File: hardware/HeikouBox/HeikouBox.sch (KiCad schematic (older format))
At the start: 93 parts, among them J1 USB_B_Micro, J103 JTAG, J2 Micro_SD_Card_Det, Q1 AO3400, Q2 AO3400, Q3 AO3400, SW1 RESET, U1 HeikouBox-Core, U2 K4S281632-UC60, U3 LD1117(1.2V), U4 LD1117(3.3V), U5 74HC04D, U6 LD1117(2.5V), U7 ATmega32U4-AU, Y1 14.31818MHz, Y2 28.37516MHz, Y3 8M

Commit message: Update to local libraries, minor work
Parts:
- U1: symbol KasaneK-Custom-Parts:HeikouBox-Core -> ksk-heikoubox:HeikouBox-Core
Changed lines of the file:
@@
 EESchema Schematic File Version 4
-LIBS:HeikouBox-cache
-EELAYER 26 0
+EELAYER 30 0
 EELAYER END
 $Descr A3 16535 11693
@@
 	6700 4300 6900 4300
 $Comp
-L KasaneK-Custom-Parts:HeikouBox-Core U1
+L ksk-heikoubox:HeikouBox-Core U1
 U 1 1 5F328BCC
 P 14200 3300
@@
 $EndComp
 $Comp
-L KasaneK-Custom-Parts:HeikouBox-Core U1
-U 2 1 5F328D2B
+L ksk-heikoubox:HeikouBox-Core U1
+U 1 1 5F328D2B
 P 14200 4900
 F 0 "U1" H 14600 5065 50  0000 C CNN
@@
 F 2 "" H 14500 4900 50  0001 C CNN
 F 3 "" H 14500 4900 50  0001 C CNN
-	2    14200 4900
-	1    0    0    -1
-$EndComp
-$Comp
-L KasaneK-Custom-Parts:HeikouBox-Core U1
-U 3 1 5F328EEB
+	1    14200 4900
+	1    0    0    -1
+$EndComp
+$Comp
+L ksk-heikoubox:HeikouBox-Core U1
+U 1 1 5F328EEB
 P 14200 6500
 F 0 "U1" H 14600 6665 50  0000 C CNN
@@
 F 2 "" H 14500 6500 50  0001 C CNN
 F 3 "" H 14500 6500 50  0001 C CNN
-	3    14200 6500
-	1    0    0    -1
-$EndComp
-$Comp
-L KasaneK-Custom-Parts:HeikouBox-Core U1
-U 4 1 5F329004
+	1    14200 6500
+	1    0    0    -1
+$EndComp
+$Comp
+L ksk-heikoubox:HeikouBox-Core U1
+U 1 1 5F329004
 P 14200 8100
 F 0 "U1" H 14600 8265 50  0000 C CNN
@@
 F 2 "" H 14500 8100 50  0001 C CNN
 F 3 "" H 14500 8100 50  0001 C CNN
-	4    14200 8100
-	1    0    0    -1
-$EndComp
+	1    14200 8100
+	1    0    0    -1
+$EndComp

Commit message: Core: Create/use overall footprint again
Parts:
- U1: symbol ksk-heikoubox:HeikouBox-Core -> KSK_HeikouBox:HeikouBox_Core
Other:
- moved on the sheet: C10, C11, C8, C9, J103, R10, R11, R12, R13, R14, R15, R16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

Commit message: Initial mainboard v1.0 schematic finished
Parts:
- removed C11: 105, symbol Device:C
- removed D3: BAT54S, Package_TO_SOT_SMD:SOT-23, symbol Diode:BAT54S
- removed JP1: 1, symbol Jumper:SolderJumper_2_Bridged
- removed JP2: 2, symbol Jumper:SolderJumper_2_Bridged
- removed JP3: 3, symbol Jumper:SolderJumper_2_Bridged
- removed JP4: 6, symbol Jumper:SolderJumper_2_Bridged
- removed JP5: 7, symbol Jumper:SolderJumper_2_Bridged
- removed Q1, Q2, Q3: AO3400, symbol Device:Q_NMOS_GSD
- removed R1: 100, symbol Device:R
- removed R3: 10K, symbol Device:R
- removed U2: K4S281632-UC60, TSOPII-54, symbol Memory_RAM:AS4C4M16SA
- removed U7: ATmega32U4-AU, Package_QFP:TQFP-44_10x10mm_P0.8mm, symbol MCU_Microchip_ATmega:ATmega32U4-AU
- added C1, C24, C25, C26, C27, C3, C31, C32, C33, C34, C35, C6, C8: 100n, symbol Device:C
- added C10, C16, C17: 10u, symbol Device:C
- added C14: 22p, symbol Device:C
- added C19: 10n, symbol Device:C
- added C21, C22, C23: 1u, symbol Device:C
- added D1: DEBUG, symbol Device:LED
- added DS1: OLED-4P-I2C, symbol KSK_HeikouBox:OLED-4P-I2C
- added F1: Poly 0.5A, symbol Device:Polyfuse_Small
- added J1: VGA, symbol Connector:DB15_Female_HighDensity_MountingHoles
- added J10: XBUS, symbol Connector_Generic:Conn_01x16
- added J2: PJ307, symbol Connector:AudioJack3_SwitchTR
- added J6: 5VDC, symbol Connector:Barrel_Jack_Switch
- added J7: Gamepad 1, symbol Connector_Generic:Conn_01x07
- added J8: Gamepad 2, symbol Connector_Generic:Conn_01x07
- added J9: Keyboard, symbol Connector:Mini-DIN-6
- added JP1: JACK - USB, symbol Jumper:SolderJumper_3_Bridged12
- added Q1, Q2, Q3, Q4, Q5, Q6, Q7: MMBT3904, Package_TO_SOT_SMD:SOT-23, symbol Transistor_BJT:MMBT3904
- added Q10, Q11, Q12, Q13, Q14, Q9: BSS138, Package_TO_SOT_SMD:SOT-23, symbol Transistor_FET:BSS138
- added Q8: MMBT3906, Package_TO_SOT_SMD:SOT-23, symbol Transistor_BJT:MMBT3906
- added R10, R105, R115, R117, R119, R121, R123, R125, R14, R15, R16, R17, R18, R19, R20, R24, R5, R52, R53, R54, R55, R56, R57, R58, R59, R6, R60, R61, R62, R7, R70, R8: 2K2, symbol Device:R
- added R100, R107, R109, R111, R113, R114, R116, R118, R120, R122, R124, R73, R74, R75, R76, R77, R78: 10K, symbol Device:R
- added R101, R102, R103, R104, R106, R108, R110, R112, R22, R4, R63, R66, R68, R72, R79, R80, R91, R92, R93, R94, R95, R96, R97, R99: 1K, symbol Device:R
- added R64: 75R, symbol Device:R
- added RV1, RV2, RV3: 1K, symbol Device:R_POT_TRIM
- added SW2: Up, symbol Switch:SW_Push
- added SW3: Select, symbol Switch:SW_Push
- added SW4: Down, symbol Switch:SW_Push
- added U2: SDRAM 128Mbit, Package_SO:TSOP-II-54_22.2x10.16mm_P0.8mm, symbol Memory_RAM:W9812G6KH-6
- added U7: ATmega644PA-AU, Package_QFP:TQFP-44_10x10mm_P0.8mm, symbol MCU_Microchip_ATmega:ATmega644PA-AU
- added U8: MCP2221AxSL, Package_SO:SOIC-14_3.9x8.7mm_P1.27mm, symbol Interface_USB:MCP2221AxSL
- C11: renamed from C12; value 220 -> 22p
- C12: renamed from C14; value 220 -> 22p
- C13: value 220 -> 22p
- C15: value 220 -> 100n
- C18: renamed from C8; value 472 -> 10n
- C2: value 106 -> 100n
- C20: renamed from C10; value 105 -> 1u
- C28: renamed from C5; value 104 -> 100n
- C29: renamed from C6; value 220 -> 22p
- C30: renamed from C7; value 220 -> 22p
- C4: value 105 -> 100n
- C5: renamed from C1; value 106 -> 10u
- C7: renamed from C3; value 106 -> 10u
- C9: value 472 -> 10u
- R1: renamed from R20; value 330K -> 1M
- R12, R13, R25: value 10K -> 2K2
- R2: value 10K -> 1K
- R21: value 100 -> 2K2
- R23: value 1K -> 75R
- R3: renamed from R21; value 330K -> 1M
- R44: value 2K2 -> 1K
- R45: value 2K2 -> 75R
- R50, R51: value 22 -> 2K2
- R65: renamed from R20; value 100 -> 1K
- R67: renamed from R24; value 10K -> 1K
- R69: renamed from R22; value 1K -> 2K2
- R71: renamed from R10; value 2K2 -> 1K
- R81: renamed from R14; value 2K2 -> 10K
- R82: renamed from R15; value 2K2 -> 10K
- R83: renamed from R16; value 2K2 -> 10K
- R84: renamed from R17; value 2K2 -> 10K
- R85: renamed from R18; value 2K2 -> 10K
- R86: renamed from R19; value 2K2 -> 10K
- R87: renamed from R4; value 2K2 -> 1K
- R88: renamed from R5; value 2K2 -> 1K
- R89: renamed from R6; value 2K2 -> 1K
- R9: value 1K -> 2K2
- R90: renamed from R7; value 2K2 -> 1K
- SW1: value RESET -> Reset; footprint Connector_PinHeader_2.54mm:PinHeader_1x02_P2.54mm_Vertical -> (none)
- U1: symbol KSK_HeikouBox:HeikouBox_Core -> KSK_HeikouBox:HeikouBox-Core
- U3: renamed from U4; value LD1117(3.3V) -> LD1117S33TR
- U4: renamed from U3; value LD1117(1.2V) -> LD1117S12TR
- U5: renamed from U6; value LD1117(2.5V) -> LD1117S25TR; symbol Regulator_Linear:LD1117S33TR_SOT223 -> Regulator_Linear:LD1117S25TR_SOT223
- U6: renamed from U5; value 74HC04D -> 74HCU04
- U6: renamed from U5; value MC74HCU04AD -> 74HCU04
- Y1: value 14.31818MHz -> 14.31818M
- Y2: value 28.37516MHz -> 28.37516M
- Y3: value 8M -> 8MHz
- renumbered D1 to D2, D2 to D3, J103 to J3, J1 to J4, J2 to J5, R8 to R98
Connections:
- net labels added: +5V, RST, SCK, SCL3, SDA3, VUSB, a_LS, a_RS, btn_D, btn_S, btn_U, c_DCLK, c_DONE, c_EN, c_NCFG, c_NSTAT, clk_14, clk_28, gp3_D1, gp3_D2, gp3_L, gp_C, gp_D1, gp_D2, gp_L, kb3_C, kb3_D, kb_C, kb_D, m_A0, m_A1, m_A10, m_A11, m_A2, m_A3, m_A4, m_A5, m_A6, m_A7, m_A8, m_A9, m_BA0, m_BA1, m_CAS, m_CKE, m_CLK, m_DQ0, m_DQ1, m_DQ10, m_DQ11, m_DQ12, m_DQ13, m_DQ14, m_DQ15, m_DQ2, m_DQ3, m_DQ4, m_DQ5, m_DQ6, m_DQ7, m_DQ8, m_DQ9, m_LDQM, m_RAS, m_UDQM, m_WE, mdb_0, mdb_1, mdb_2, mdb_3, mdb_4, mdb_4H, mdb_5, mdb_6, mdb_7, sd_CS, u_CH, u_HC, u_HC_CK, u_HP, u_PH, v_BLU0, v_BLU1, v_BLU2, v_BLU3, v_BLU4, v_GRN0, v_GRN1, v_GRN2, v_GRN3, v_GRN4, v_GRN5, v_IN0, v_IN1, v_IN10, v_IN11, v_IN12, v_IN13, v_IN14, v_IN15, v_IN2, v_IN3, v_IN4, v_IN5, v_IN6, v_IN7, v_IN8, v_IN9, v_NHS, v_NVS, v_RED0, v_RED1, v_RED2, v_RED3, v_RED4
- net labels removed: AUD_L, AUD_R, BLU0, BLU1, BLU2, BLU3, BLU4, BTN, CLK_14M, CLK_28M, C_CFG, C_CLK, C_CS, C_DAT, C_DONE, C_STAT, E_SCL, E_SDA, GRN0, GRN1, GRN2, GRN3, GRN4, GRN5, HSYNC, MDB0, MDB1, MDB2, MDB3, MDB4, MDB5, MDB6, MDB7, RED0, RED1, RED2, RED3, RED4, RXLED, R_A0, R_A1, R_A10, R_A11, R_A2, R_A3, R_A4, R_A5, R_A6, R_A7, R_A8, R_A9, R_BA0, R_BA1, R_CAS, R_CKE, R_CLK, R_D0, R_D1, R_D10, R_D11, R_D12, R_D13, R_D14, R_D15, R_D2, R_D3, R_D4, R_D5, R_D6, R_D7, R_D8, R_D9, R_DQMH, R_DQML, R_RAS, R_WE, S0, S1, S2, S3, SCLK, SD_CS, SD_DET, SIGMA_L, SIGMA_R, TXLED, U_RX, U_TX, VBUS, VIN_0, VIN_1, VIN_10, VIN_11, VIN_12, VIN_13, VIN_14, VIN_15, VIN_2, VIN_3, VIN_4, VIN_5, VIN_6, VIN_7, VIN_8, VIN_9, VSYNC
- wire segments 534 -> 700
- no-connect marks 8 -> 23
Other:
- note added: "1. Core"
- note added: "10. SD Card"
- note added: "11. Config Interface Overlay"
- note added: "12. Display"
- note added: "13. Buttons"
- note added: "14. Power Input"
- note added: "15. IO Level Shifting"
- note added: "16. Gamepad Interface"
- note added: "17. PS/2 Keyboard Interface"
- note added: "18. Extra pins Breakout"
- note added: "2. Memory"
- note added: "3. Power Rails"
- note added: "4. Core Clock Oscillators"
- note added: "5. VGA Buffer"
- note added: "6. Audio Filter & Buffer"
- note added: "7. JTAG & Cfg Pullup"
- note added: "8. Hub (MCU)"
- note added: "9. USB Interface"
- note added: "IO"
- note added: "Mind LDQM\n/ UDQM in\nDQ remap!"
- note added: "Stability not guaranteed with low ESR output caps"
- note added: "To 10K\nline input"
- note removed: "ADD AUDIO AMP AND OUTPUT"
- note removed: "HSYNC OUT"
- note removed: "R12/13 CROSS CONFIGURATION"
- note removed: "VSYNC OUT"
- moved on the sheet: C11, C12, C18, C20, C28, C29, C30, C5, C7, D2, D3, J3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

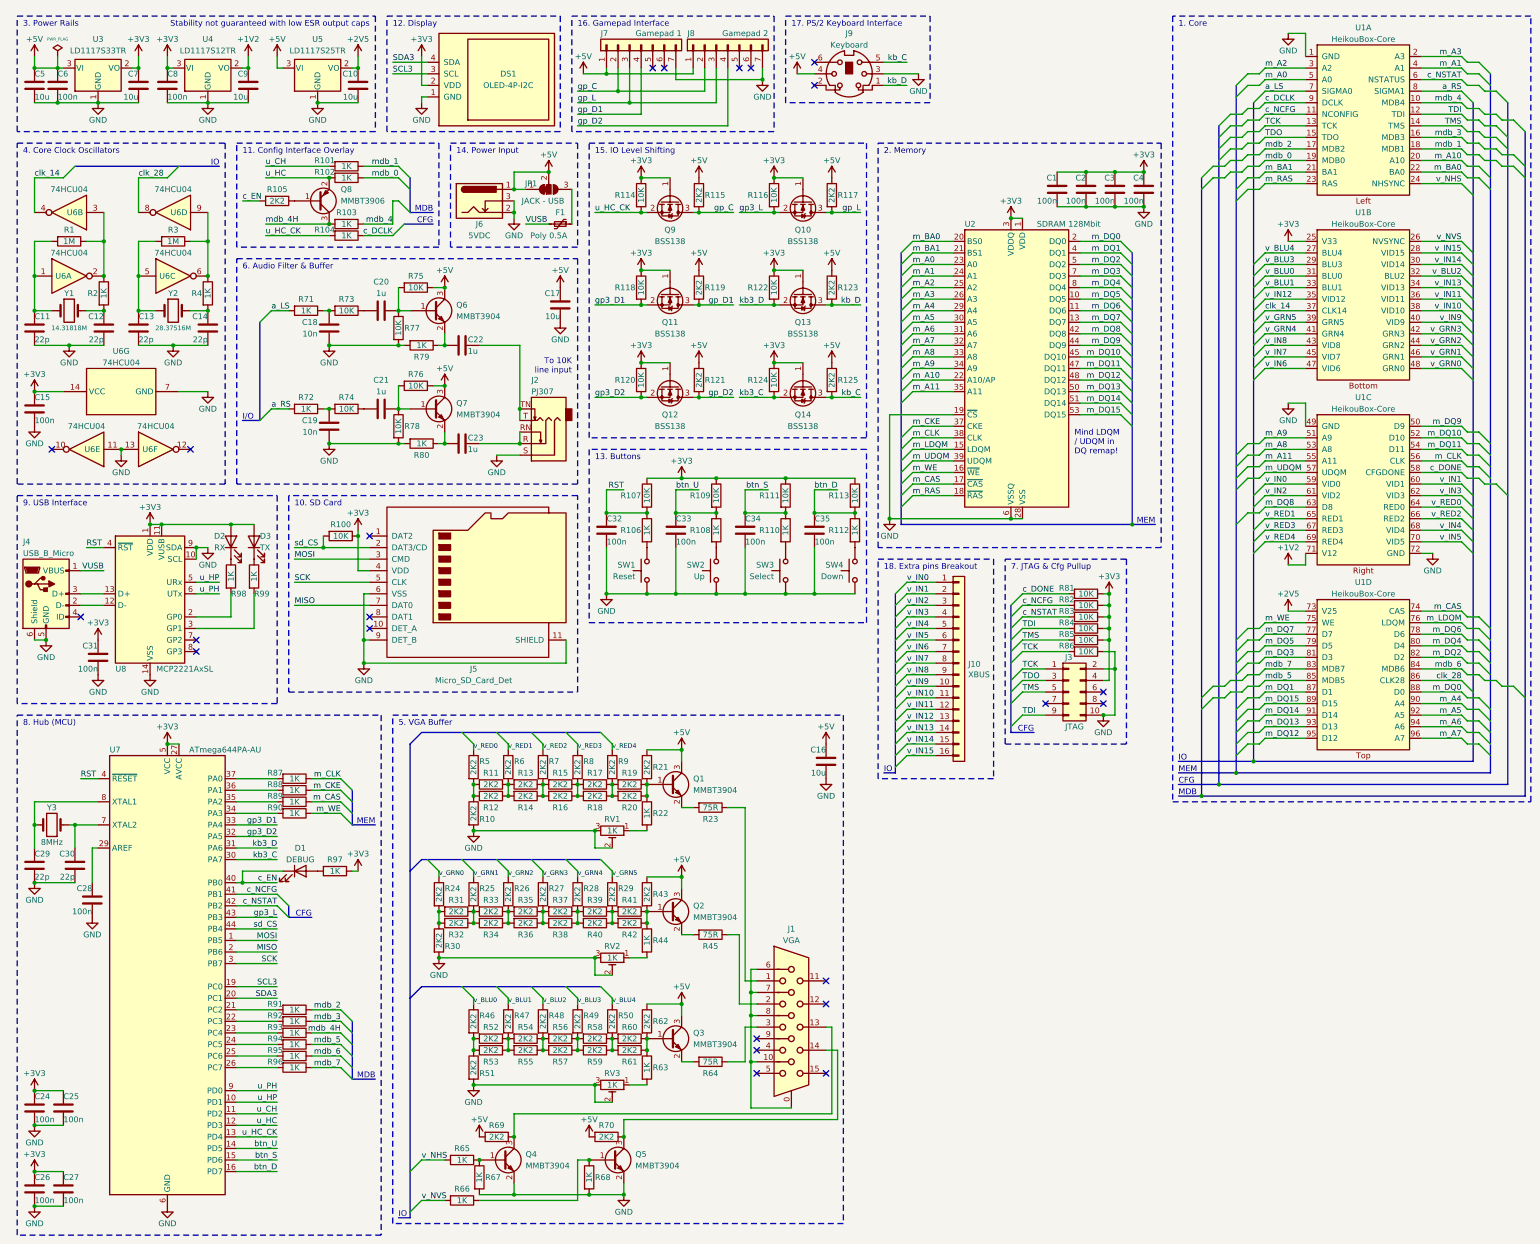
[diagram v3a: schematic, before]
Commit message: Tidy up and split to multi sheet
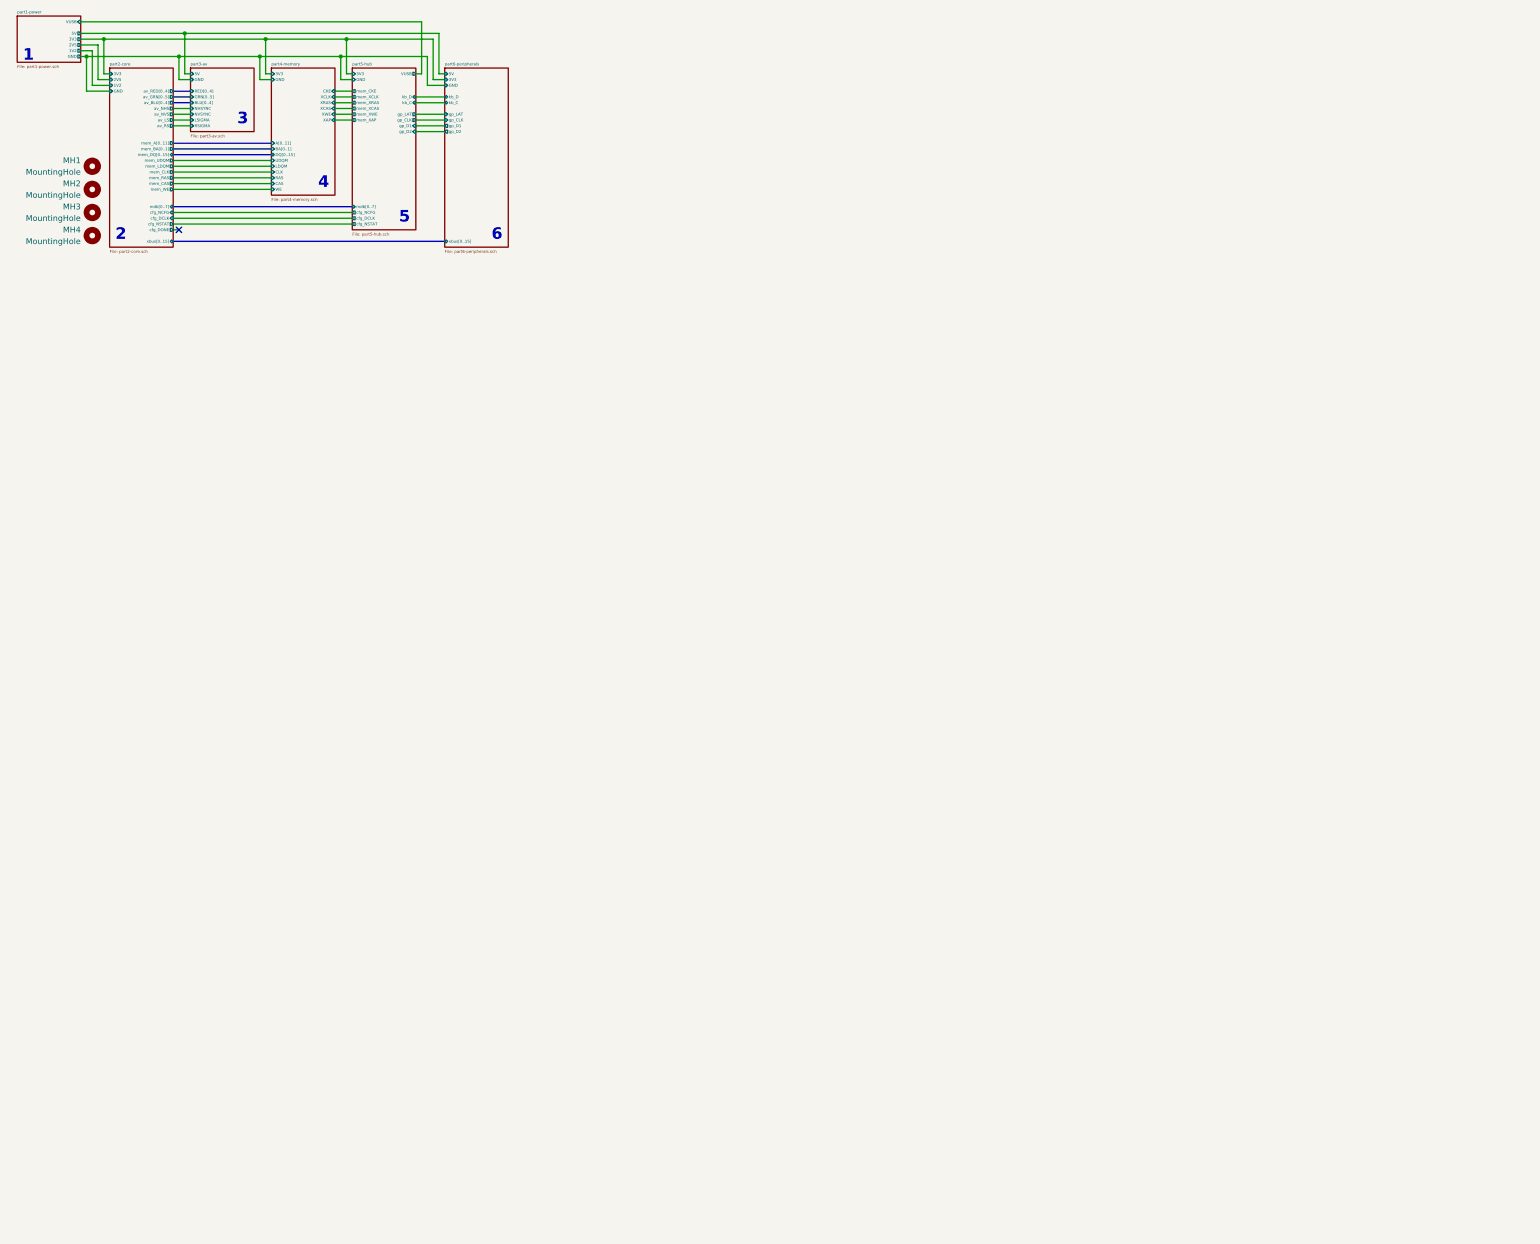
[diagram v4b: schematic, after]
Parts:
- removed C1, C15, C2, C24, C25, C26, C27, C28, C3, C31, C32, C33, C34, C35, C4, C6, C8: 100n, symbol Device:C
- removed C10, C16, C17, C5, C7, C9: 10u, symbol Device:C
- removed C11, C12, C13, C14, C29, C30: 22p, symbol Device:C
- removed C18, C19: 10n, symbol Device:C
- removed C20, C21, C22, C23: 1u, symbol Device:C
- removed D1: DEBUG, symbol Device:LED
- removed D2: RX, symbol Device:LED
- removed D3: TX, symbol Device:LED
- removed DS1: OLED-4P-I2C, symbol KSK_HeikouBox:OLED-4P-I2C
- removed F1: Poly 0.5A, symbol Device:Polyfuse_Small
- removed J1: VGA, symbol Connector:DB15_Female_HighDensity_MountingHoles
- removed J10: XBUS, symbol Connector_Generic:Conn_01x16
- removed J2: PJ307, symbol Connector:AudioJack3_SwitchTR
- removed J3: JTAG, symbol Connector_Generic:Conn_02x05_Odd_Even
- removed J4: USB_B_Micro, symbol Connector:USB_B_Micro
- removed J5: Micro_SD_Card_Det, symbol Connector:Micro_SD_Card_Det
- removed J6: 5VDC, symbol Connector:Barrel_Jack_Switch
- removed J7: Gamepad 1, symbol Connector_Generic:Conn_01x07
- removed J8: Gamepad 2, symbol Connector_Generic:Conn_01x07
- removed J9: Keyboard, symbol Connector:Mini-DIN-6
- removed JP1: JACK - USB, symbol Jumper:SolderJumper_3_Bridged12
- removed Q1, Q2, Q3, Q4, Q5, Q6, Q7: MMBT3904, Package_TO_SOT_SMD:SOT-23, symbol Transistor_BJT:MMBT3904
- removed Q10, Q11, Q12, Q13, Q14, Q9: BSS138, Package_TO_SOT_SMD:SOT-23, symbol Transistor_FET:BSS138
- removed Q8: MMBT3906, Package_TO_SOT_SMD:SOT-23, symbol Transistor_BJT:MMBT3906
- removed R1, R3: 1M, symbol Device:R
- removed R10, R105, R11, R115, R117, R119, R12, R121, R123, R125, R13, R14, R15, R16, R17, R18, R19, R20, R21, R24, R25, R26, R27, R28, R29, R30, R31, R32, R33, R34, R35, R36, R37, R38, R39, R40, R41, R42, R43, R46, R47, R48, R49, R5, R50, R51, R52, R53, R54, R55, R56, R57, R58, R59, R6, R60, R61, R62, R69, R7, R70, R8, R9: 2K2, symbol Device:R
- removed R100, R107, R109, R111, R113, R114, R116, R118, R120, R122, R124, R73, R74, R75, R76, R77, R78, R81, R82, R83, R84, R85, R86: 10K, symbol Device:R
- removed R101, R102, R103, R104, R106, R108, R110, R112, R2, R22, R4, R44, R63, R65, R66, R67, R68, R71, R72, R79, R80, R87, R88, R89, R90, R91, R92, R93, R94, R95, R96, R97, R98, R99: 1K, symbol Device:R
- removed R23, R45, R64: 75R, symbol Device:R
- removed RV1, RV2, RV3: 1K, symbol Device:R_POT_TRIM
- removed SW1: Reset, symbol Switch:SW_Push
- removed SW2: Up, symbol Switch:SW_Push
- removed SW3: Select, symbol Switch:SW_Push
- removed SW4: Down, symbol Switch:SW_Push
- removed U1: HeikouBox-Core, symbol KSK_HeikouBox:HeikouBox-Core
- removed U2: SDRAM 128Mbit, Package_SO:TSOP-II-54_22.2x10.16mm_P0.8mm, symbol Memory_RAM:W9812G6KH-6
- removed U3: LD1117S33TR, Package_TO_SOT_SMD:SOT-223-3_TabPin2, symbol Regulator_Linear:LD1117S33TR_SOT223
- removed U4: LD1117S12TR, Package_TO_SOT_SMD:SOT-223-3_TabPin2, symbol Regulator_Linear:LD1117S12TR_SOT223
- removed U5: LD1117S25TR, Package_TO_SOT_SMD:SOT-223-3_TabPin2, symbol Regulator_Linear:LD1117S25TR_SOT223
- removed U6: 74HCU04, symbol 74xx:74HC04
- removed U7: ATmega644PA-AU, Package_QFP:TQFP-44_10x10mm_P0.8mm, symbol MCU_Microchip_ATmega:ATmega644PA-AU
- removed U8: MCP2221AxSL, Package_SO:SOIC-14_3.9x8.7mm_P1.27mm, symbol Interface_USB:MCP2221AxSL
- removed Y1: 14.31818M, symbol Device:Crystal
- removed Y2: 28.37516M, symbol Device:Crystal
- removed Y3: 8MHz, symbol Device:Crystal
- added MH1, MH2, MH3, MH4: MountingHole, MountingHole:MountingHole_3.2mm_M3, symbol Mechanical:MountingHole
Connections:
- no-connect marks 23 -> 1
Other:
- note added: "1"
- note added: "2"
- note added: "3"
- note added: "4"
- note added: "5"
- note added: "6"
- note removed: "1. Core"
- note removed: "10. SD Card"
- note removed: "11. Config Interface Overlay"
- note removed: "12. Display"
- note removed: "13. Buttons"
- note removed: "14. Power Input"
- note removed: "15. IO Level Shifting"
- note removed: "16. Gamepad Interface"
- note removed: "17. PS/2 Keyboard Interface"
- note removed: "18. Extra pins Breakout"
- note removed: "2. Memory"
- note removed: "3. Power Rails"
- note removed: "4. Core Clock Oscillators"
- note removed: "5. VGA Buffer"
- note removed: "6. Audio Filter & Buffer"
- note removed: "7. JTAG & Cfg Pullup"
- note removed: "8. Hub (MCU)"
- note removed: "9. USB Interface"
- note removed: "CFG"
- note removed: "I/O"
- note removed: "IO"
- note removed: "MDB"
- note removed: "MEM"
- note removed: "Mind LDQM\n/ UDQM in\nDQ remap!"
- note removed: "Stability not guaranteed with low ESR output caps"
- note removed: "To 10K\nline input"

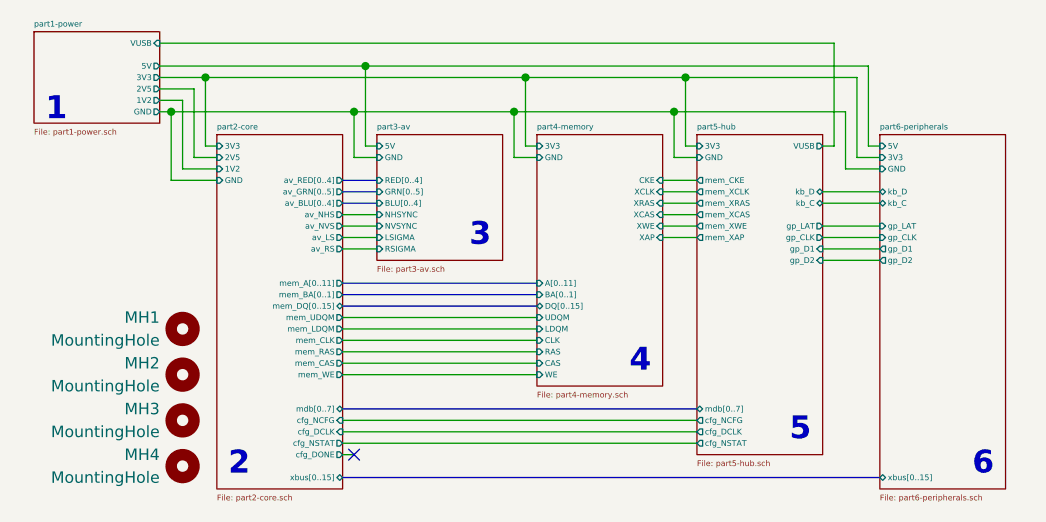
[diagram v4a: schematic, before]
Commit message: Replace MCU with blue pill, tidy up
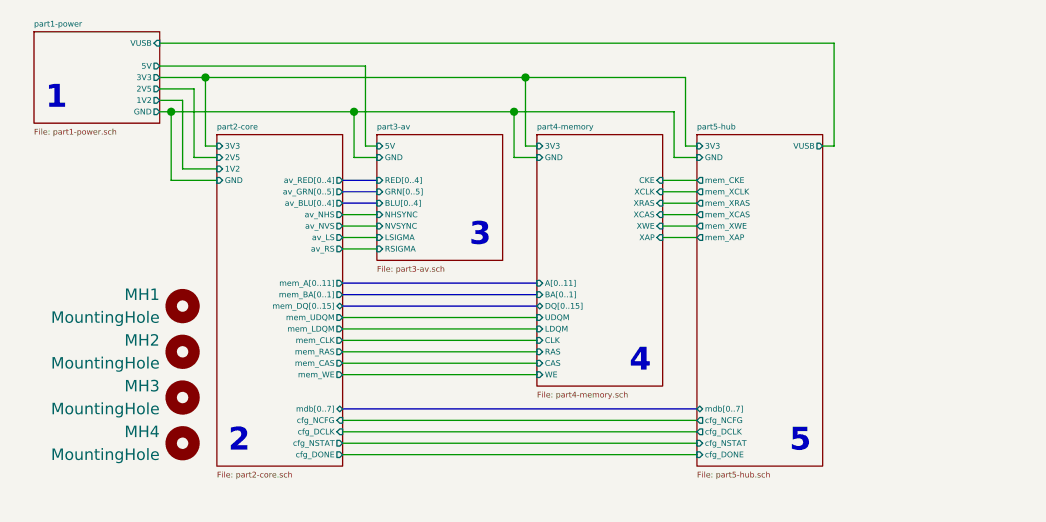
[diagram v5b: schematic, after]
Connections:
- no-connect marks 1 -> 0
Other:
- note removed: "6"
- moved on the sheet: MH1, MH2, MH3, MH4
